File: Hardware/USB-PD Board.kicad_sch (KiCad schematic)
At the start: 52 parts, among them J1 USB_C_Receptacle, J2 Conn_01x04_Male, J3 Conn_01x02_Male, J4 Conn_01x02_Male, J5 Conn_01x02_Male, J6 Conn_01x02_Male, J7 Conn_01x08_Male, J9 QWIIC_Stackable, Q1 DMP3013SFV, Q2 DMP3013SFV, SW1 SW_Push, U1 STUSB4500QTR, U2 R1501J033B-T1-JE

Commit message: Uber Rework!
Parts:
- J2: footprint Tinker:PinHeader_1x04_P2.54mm_Vertical -> Tinker:Board_Stacker_4
- J3, J4, J5, J6: footprint Tinker:PinHeader_1x02_P2.54mm_Vertical -> Tinker:Board_Stacker_2
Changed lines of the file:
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@@
   (title_block
     (title "USB-C (PD) Board")
-    (rev "0.0.9")
+    (rev "0.1.9")
     (company "The Nerd Mage")
     (comment 1 "Set I2C address by cutting 1 or both links in JP5")
@@
     (property "Reference" "J3" (id 0) (at 59.055 97.79 0))
     (property "Value" "Conn_01x02_Male" (id 1) (at 59.055 100.33 0))
-    (property "Footprint" "Tinker:PinHeader_1x02_P2.54mm_Vertical" (id 2) (at 59.69 102.87 0)
+    (property "Footprint" "Tinker:Board_Stacker_2" (id 2) (at 59.69 102.87 0)
       (effects (font (size 1.27 1.27)) hide)
     )
@@
     (property "Reference" "J4" (id 0) (at 59.055 111.76 0))
     (property "Value" "Conn_01x02_Male" (id 1) (at 59.055 114.3 0))
-    (property "Footprint" "Tinker:PinHeader_1x02_P2.54mm_Vertical" (id 2) (at 59.69 116.84 0)
+    (property "Footprint" "Tinker:Board_Stacker_2" (id 2) (at 59.69 116.84 0)
       (effects (font (size 1.27 1.27)) hide)
     )
@@
       (effects (font (size 1.27 1.27)) (justify right))
     )
-    (property "Footprint" "Tinker:PinHeader_1x04_P2.54mm_Vertical" (id 2) (at 68.58 69.85 0)
+    (property "Footprint" "Tinker:Board_Stacker_4" (id 2) (at 68.58 69.85 0)
       (effects (font (size 1.27 1.27)) hide)
     )
@@
       (effects (font (size 1.27 1.27)) (justify right))
     )
-    (property "Footprint" "Tinker:PinHeader_1x02_P2.54mm_Vertical" (id 2) (at 92.71 158.75 0)
+    (property "Footprint" "Tinker:Board_Stacker_2" (id 2) (at 92.71 158.75 0)
       (effects (font (size 1.27 1.27)) hide)
     )
@@
     (property "Reference" "J5" (id 0) (at 92.075 139.7 0))
     (property "Value" "Conn_01x02_Male" (id 1) (at 92.075 142.24 0))
-    (property "Footprint" "Tinker:PinHeader_1x02_P2.54mm_Vertical" (id 2) (at 92.71 144.78 0)
+    (property "Footprint" "Tinker:Board_Stacker_2" (id 2) (at 92.71 144.78 0)
       (effects (font (size 1.27 1.27)) hide)
     )
@@
     )
     (path "/ce562b82-4d15-4512-9ef8-80a89b06889d"
-      (reference "J2") (unit 1) (value "Conn_01x04_Male") (footprint "Tinker:PinHeader_1x04_P2.54mm_Vertical")
+      (reference "J2") (unit 1) (value "Conn_01x04_Male") (footprint "Tinker:Board_Stacker_4")
     )
     (path "/31399746-8e56-4d74-b787-07c634e0c687"
-      (reference "J3") (unit 1) (value "Conn_01x02_Male") (footprint "Tinker:PinHeader_1x02_P2.54mm_Vertical")
+      (reference "J3") (unit 1) (value "Conn_01x02_Male") (footprint "Tinker:Board_Stacker_2")
     )
     (path "/4b9f3ca1-fb99-4af6-a9fd-ecb98c706083"
-      (reference "J4") (unit 1) (value "Conn_01x02_Male") (footprint "Tinker:PinHeader_1x02_P2.54mm_Vertical")
+      (reference "J4") (unit 1) (value "Conn_01x02_Male") (footprint "Tinker:Board_Stacker_2")
     )
     (path "/fb3406f1-7439-4c3c-b07d-423418b2c3c6"
-      (reference "J5") (unit 1) (value "Conn_01x02_Male") (footprint "Tinker:PinHeader_1x02_P2.54mm_Vertical")
+      (reference "J5") (unit 1) (value "Conn_01x02_Male") (footprint "Tinker:Board_Stacker_2")
     )
     (path "/d2bacdbb-6a99-475b-b165-ccef827277cd"
-      (reference "J6") (unit 1) (value "Conn_01x02_Male") (footprint "Tinker:PinHeader_1x02_P2.54mm_Vertical")
+      (reference "J6") (unit 1) (value "Conn_01x02_Male") (footprint "Tinker:Board_Stacker_2")
     )
     (path "/83fa4a07-5e65-4e04-a1b2-4b4ecccd45bd"

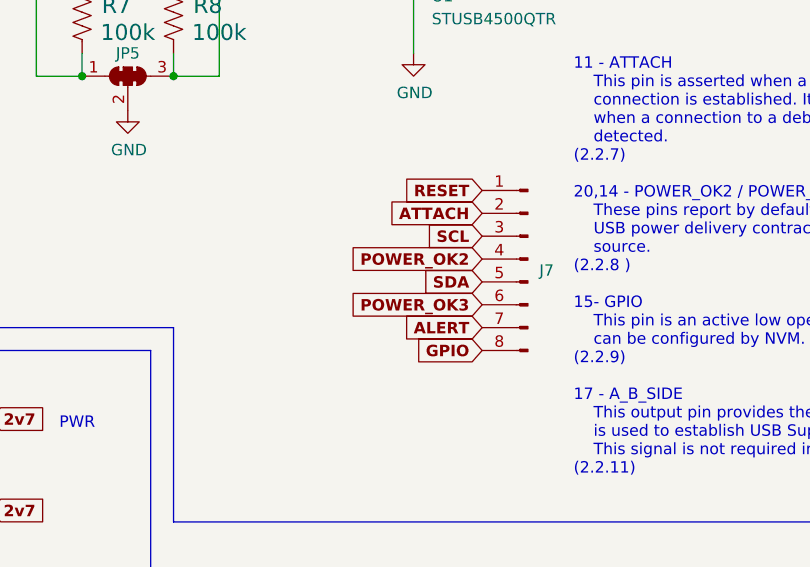
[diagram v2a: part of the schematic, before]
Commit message: Making J7 I2C + SPI only...
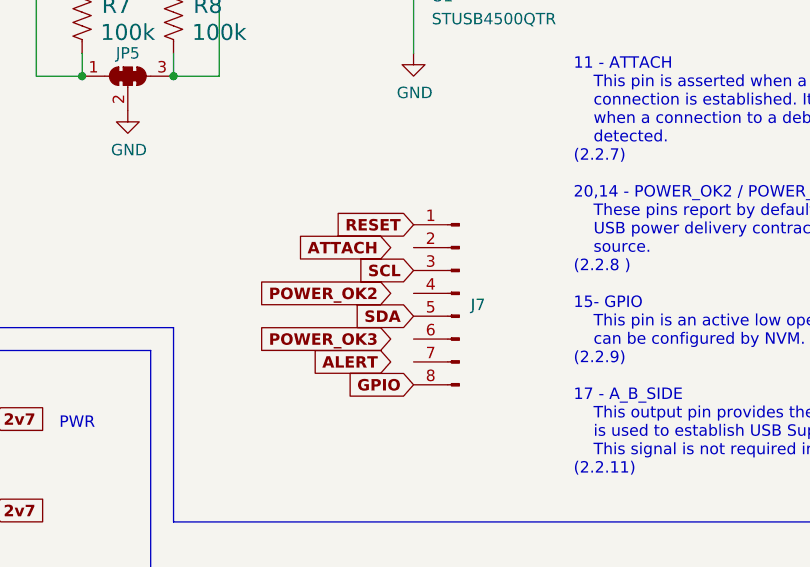
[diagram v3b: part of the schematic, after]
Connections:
- net ALERT: no longer J7.7 (Pin_7)
- net ATTACH: no longer J7.2 (Pin_2)
- net POWER_OK2: no longer J7.4 (Pin_4)
- net POWER_OK3: no longer J7.6 (Pin_6)
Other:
- moved on the sheet: J7
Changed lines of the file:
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@@
     )
   )
-  (global_label "SDA" (shape input) (at 212.09 137.16 180) (fields_autoplaced)
+  (global_label "SDA" (shape input) (at 204.47 140.97 180) (fields_autoplaced)
     (effects (font (size 1.27 1.27) bold) (justify right))
-    (property "Intersheet References" "${INTERSHEET_REFS}" (id 0) (at 205.9184 137.033 0)
+    (property "Intersheet References" "${INTERSHEET_REFS}" (id 0) (at 198.2984 140.843 0)
       (effects (font (size 1.27 1.27) bold) (justify right) hide)
     )
@@
     )
   )
-  (global_label "RESET" (shape input) (at 212.09 127 180) (fields_autoplaced)
+  (global_label "RESET" (shape input) (at 204.47 130.81 180) (fields_autoplaced)
     (effects (font (size 1.27 1.27) (thickness 0.254) bold) (justify right))
-    (property "Intersheet References" "${INTERSHEET_REFS}" (id 0) (at 203.7413 126.873 0)
+    (property "Intersheet References" "${INTERSHEET_REFS}" (id 0) (at 196.1213 130.683 0)
       (effects (font (size 1.27 1.27) (thickness 0.254) bold) (justify right) hide)
     )
@@
     )
   )
-  (global_label "SCL" (shape input) (at 212.09 132.08 180) (fields_autoplaced)
+  (global_label "SCL" (shape input) (at 204.47 135.89 180) (fields_autoplaced)
     (effects (font (size 1.27 1.27) (thickness 0.254) bold) (justify right))
-    (property "Intersheet References" "${INTERSHEET_REFS}" (id 0) (at 205.9789 131.953 0)
+    (property "Intersheet References" "${INTERSHEET_REFS}" (id 0) (at 198.3589 135.763 0)
       (effects (font (size 1.27 1.27) (thickness 0.254) bold) (justify right) hide)
     )
@@
     )
   )
-  (global_label "POWER_OK3" (shape input) (at 212.09 139.7 180) (fields_autoplaced)
+  (global_label "POWER_OK3" (shape input) (at 201.93 143.51 180) (fields_autoplaced)
     (effects (font (size 1.27 1.27) (thickness 0.254) bold) (justify right))
-    (property "Intersheet References" "${INTERSHEET_REFS}" (id 0) (at 198.2379 139.573 0)
+    (property "Intersheet References" "${INTERSHEET_REFS}" (id 0) (at 188.0779 143.383 0)
       (effects (font (size 1.27 1.27) (thickness 0.254) bold) (justify right) hide)
     )
@@
     )
   )
-  (global_label "ATTACH" (shape input) (at 212.09 129.54 180) (fields_autoplaced)
+  (global_label "ATTACH" (shape input) (at 201.93 133.35 180) (fields_autoplaced)
     (effects (font (size 1.27 1.27) (thickness 0.254) bold) (justify right))
-    (property "Intersheet References" "${INTERSHEET_REFS}" (id 0) (at 202.7736 129.413 0)
+    (property "Intersheet References" "${INTERSHEET_REFS}" (id 0) (at 192.6136 133.223 0)
       (effects (font (size 1.27 1.27) (thickness 0.254) bold) (justify right) hide)
     )
@@
     )
   )
-  (global_label "ALERT" (shape input) (at 212.09 142.24 180) (fields_autoplaced)
+  (global_label "ALERT" (shape input) (at 201.93 146.05 180) (fields_autoplaced)
     (effects (font (size 1.27 1.27) bold) (justify right))
-    (property "Intersheet References" "${INTERSHEET_REFS}" (id 0) (at 203.9832 142.113 0)
+    (property "Intersheet References" "${INTERSHEET_REFS}" (id 0) (at 193.8232 145.923 0)
       (effects (font (size 1.27 1.27) bold) (justify right) hide)
     )
@@
     )
   )
-  (global_label "POWER_OK2" (shape input) (at 212.09 134.62 180) (fields_autoplaced)
+  (global_label "POWER_OK2" (shape input) (at 201.93 138.43 180) (fields_autoplaced)
     (effects (font (size 1.27 1.27) (thickness 0.254) bold) (justify right))
-    (property "Intersheet References" "${INTERSHEET_REFS}" (id 0) (at 198.2379 134.493 0)
+    (property "Intersheet References" "${INTERSHEET_REFS}" (id 0) (at 188.0779 138.303 0)
       (effects (font (size 1.27 1.27) (thickness 0.254) bold) (justify right) hide)
     )
@@
     )
   )
-  (global_label "GPIO" (shape input) (at 212.09 144.78 180) (fields_autoplaced)
+  (global_label "GPIO" (shape input) (at 204.47 148.59 180) (fields_autoplaced)
     (effects (font (size 1.27 1.27) (thickness 0.254) bold) (justify right))
-    (property "Intersheet References" "${INTERSHEET_REFS}" (id 0) (at 205.0113 144.653 0)
+    (property "Intersheet References" "${INTERSHEET_REFS}" (id 0) (at 197.3913 148.463 0)
       (effects (font (size 1.27 1.27) (thickness 0.254) bold) (justify right) hide)
     )
@@
     (pin "1")
   )
-  (symbol (lib_id "Connector:Conn_01x08_Male") (at 217.17 134.62 0) (mirror y) (unit 1)
+  (symbol (lib_id "Connector:Conn_01x08_Male") (at 209.55 138.43 0) (mirror y) (unit 1)
     (in_bom yes) (on_board yes) (fields_autoplaced)
-    (property "Reference" "J7" (id 0) (at 218.44 135.8899 0)
+    (property "Reference" "J7" (id 0) (at 210.82 139.6999 0)
       (effects (font (size 1.27 1.27)) (justify right))
     )
-    (property "Value" "Conn_01x08_Male" (id 1) (at 218.44 137.1599 0)
-      (effects (font (size 1.27 1.27)) (justify right) hide)
-    )
-    (property "Footprint" "Tinker:PinHeader_2x04_P1.27mm_Vertical" (id 2) (at 217.17 134.62 0)
-      (effects (font (size 1.27 1.27)) hide)
-    )
-    (property "Datasheet" "~" (id 3) (at 217.17 134.62 0)
-      (effects (font (size 1.27 1.27)) hide)
-    )
-    (property "LCSC" "C2881786 + C2684732" (id 4) (at 217.17 134.62 0)
-      (effects (font (size 1.27 1.27)) hide)
-    )
+    (property "Value" "Conn_01x08_Male" (id 1) (at 210.82 140.9699 0)
+      (effects (font (size 1.27 1.27)) (justify right) hide)
+    )
+    (property "Footprint" "Tinker:PinHeader_2x04_P1.27mm_Vertical" (id 2) (at 209.55 138.43 0)
+      (effects (font (size 1.27 1.27)) hide)
+    )
+    (property "Datasheet" "~" (id 3) (at 209.55 138.43 0)
+      (effects (font (size 1.27 1.27)) hide)
+    )
+    (property "LCSC" "C2881786 + C2684732" (id 4) (at 209.55 138.43 0)
+      (effects (font (size 1.27 1.27)) hide)
+    )

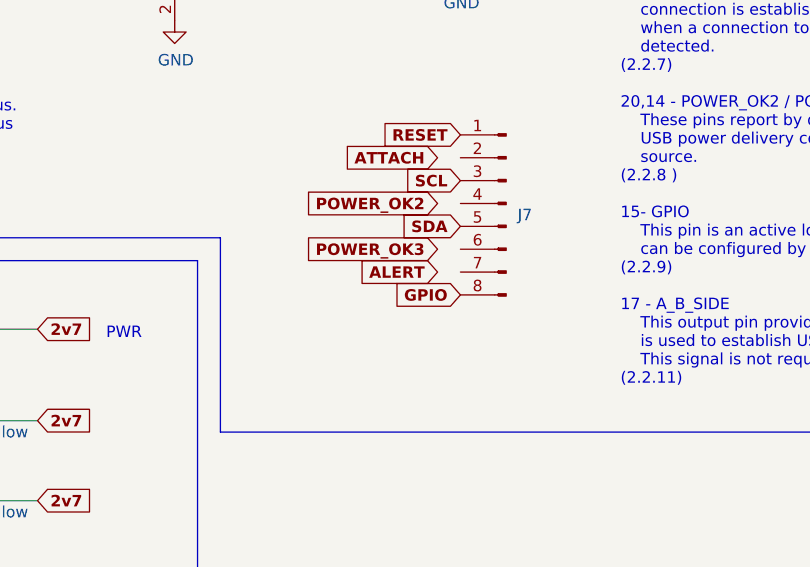
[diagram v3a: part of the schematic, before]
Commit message: Still cleaning up J7
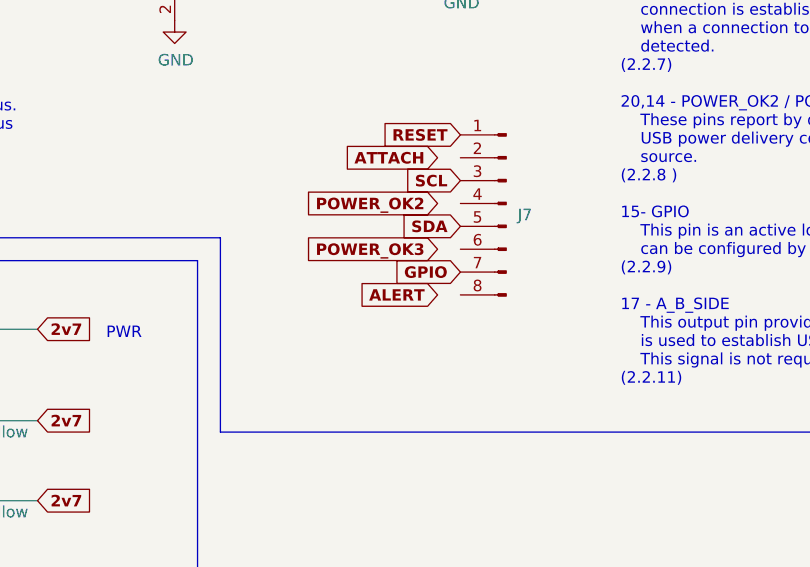
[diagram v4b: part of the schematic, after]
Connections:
- net GPIO: now also J7.7 (Pin_7); no longer J7.8 (Pin_8)
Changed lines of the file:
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@@
     )
   )
-  (global_label "ALERT" (shape input) (at 201.93 146.05 180) (fields_autoplaced)
+  (global_label "ALERT" (shape input) (at 201.93 148.59 180) (fields_autoplaced)
     (effects (font (size 1.27 1.27) bold) (justify right))
-    (property "Intersheet References" "${INTERSHEET_REFS}" (id 0) (at 193.8232 145.923 0)
+    (property "Intersheet References" "${INTERSHEET_REFS}" (id 0) (at 193.8232 148.463 0)
       (effects (font (size 1.27 1.27) bold) (justify right) hide)
     )
@@
     )
   )
-  (global_label "GPIO" (shape input) (at 204.47 148.59 180) (fields_autoplaced)
+  (global_label "GPIO" (shape input) (at 204.47 146.05 180) (fields_autoplaced)
     (effects (font (size 1.27 1.27) (thickness 0.254) bold) (justify right))
-    (property "Intersheet References" "${INTERSHEET_REFS}" (id 0) (at 197.3913 148.463 0)
+    (property "Intersheet References" "${INTERSHEET_REFS}" (id 0) (at 197.3913 145.923 0)
       (effects (font (size 1.27 1.27) (thickness 0.254) bold) (justify right) hide)
     )

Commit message: Still migrating to 0.2.x
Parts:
- removed JP2, JP3, JP4: SolderJumper_2_Bridged, Tinker:SolderJumper-2_P_Bridged_Rounded_skinny, symbol Jumper:SolderJumper_2_Bridged
- C1: LCSC C89246 -> C145122
- J9: footprint Tinker:QWIIC_Stackable -> Tinker:QWIIC_Stack_II; LCSC C145956 -> (none)
- renumbered R8 to R12, R7 to R13, R6 to R14, R9 to R18, R18 to R6, R12 to R7, R13 to R8, R14 to R9
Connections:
- net 2v7: now also R3.2, R4.2, R5.2
- net ADDR0: now also JP5.3 (B), R12.1; no longer JP5.1 (A), R13.1
- net ADDR1: now also JP5.1 (A), R13.1; no longer JP5.3 (B), R12.1
- net GPIO: no longer J7.7 (Pin_7)
- net RESET: now also J7.2 (Pin_2); no longer J7.1 (Pin_1)
- net SCL: no longer J7.3 (Pin_3)
- net SDA: no longer J7.5 (Pin_5)
- net SCLK: now reaches J7.4 (Pin_4)
- net MISO: now reaches J7.6 (Pin_6)
- net MOSI: now reaches J7.8 (Pin_8)
- new net ~{RESET}: J7.1 (Pin_1)
- new net ~{SCS}0: J7.7 (Pin_7)
- new net ~{SCS}1: J7.5 (Pin_5)
- new net ~{SCS}2: J7.3 (Pin_3)
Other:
- moved on the sheet: J7, JP5, R12, R13
